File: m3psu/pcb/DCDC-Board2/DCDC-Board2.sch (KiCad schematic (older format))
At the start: 6 parts, among them J1 WEST TOP, J2 WEST BOT, J3 NORTH TOP, J4 EAST TOP, J5 EAST BOT, J6 NORTH BOT

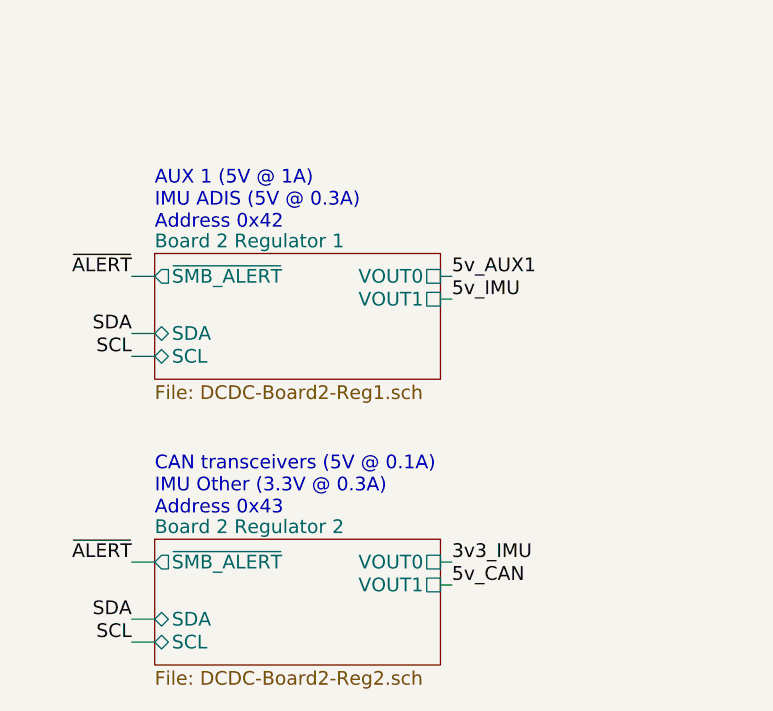
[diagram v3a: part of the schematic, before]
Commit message: create DCDC1/2/3 from prototype
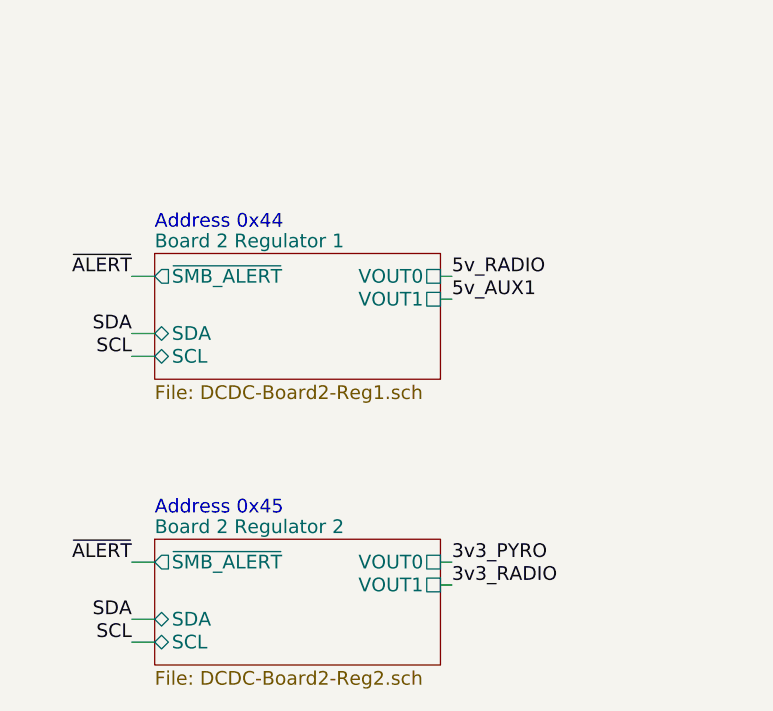
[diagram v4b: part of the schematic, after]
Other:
- note added: "Address 0x44"
- note added: "Address 0x45"
- note removed: "AUX 1 (5V @ 1A)\nIMU ADIS (5V @ 0.3A)\nAddress 0x42"
- note removed: "CAN transceivers (5V @ 0.1A)\nIMU Other (3.3V @ 0.3A)\nAddress 0x43"
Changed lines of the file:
@@
 $EndDescr
 Text Notes 5100 2800 0    60   ~ 0
-AUX 1 (5V @ 1A)\nIMU ADIS (5V @ 0.3A)\nAddress 0x42
+Address 0x44
 Text Notes 5100 4050 0    60   ~ 0
-CAN transceivers (5V @ 0.1A)\nIMU Other (3.3V @ 0.3A)\nAddress 0x43
+Address 0x45
 $Sheet
 S 5100 2900 1250 550
@@
 Text Label 5000 3250 2    60   ~ 0
 SDA
-Text Label 6400 3000 0    60   ~ 0
-5v_AUX1
-Text Label 6400 4350 0    60   ~ 0
-5v_CAN
 Wire Wire Line
 	5000 3250 5100 3250
@@
 Wire Wire Line
 	5100 4600 5000 4600
-Text Label 6400 4250 0    60   ~ 0
-3v3_IMU
-Text Label 6400 3100 0    60   ~ 0
-5v_IMU
 Wire Wire Line
 	5100 3000 5000 3000
@@
 Text Label 10300 4200 2    60   ~ 0
 JTDO
+Text Label 6400 3000 0    60   ~ 0
+5v_RADIO
+Text Label 6400 3100 0    60   ~ 0
+5v_AUX1
+Text Label 6400 4350 0    60   ~ 0
+3v3_RADIO
+Text Label 6400 4250 0    60   ~ 0
+3v3_PYRO
 $EndSCHEMATC

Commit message: update DCDC address setting resistors due to making DCDC2 with DCDC1's resistors (intentionally)
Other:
- note added: "Address 0x42"
- note added: "Address 0x43"
- note removed: "Address 0x44"
- note removed: "Address 0x45"
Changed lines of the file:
@@
 $EndDescr
 Text Notes 5100 2800 0    60   ~ 0
-Address 0x44
+Address 0x42
 Text Notes 5100 4050 0    60   ~ 0
-Address 0x45
+Address 0x43
 $Sheet
 S 5100 2900 1250 550
